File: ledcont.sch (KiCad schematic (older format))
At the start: 22 parts, among them J1 Screw_Terminal_01x02, J2 Screw_Terminal_01x02, U1 PAM2804, U2 TSM102A

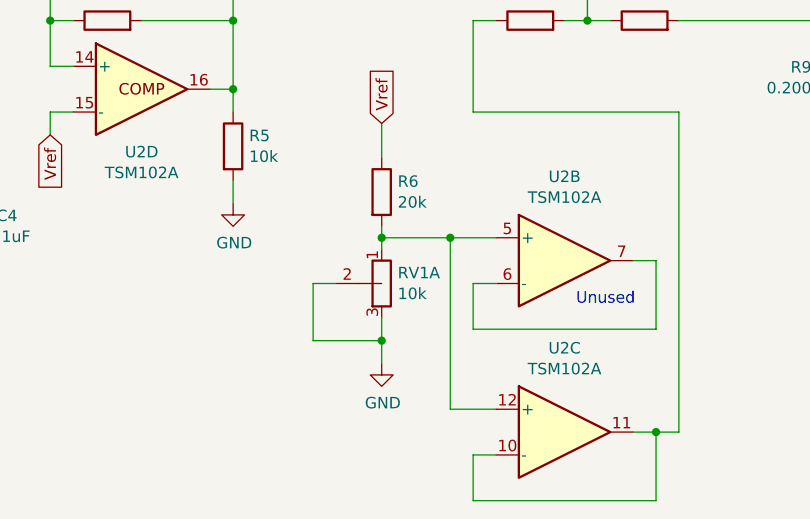
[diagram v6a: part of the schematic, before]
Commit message: Reverse potentionmeter usage so that the LEDs start out dimmed.
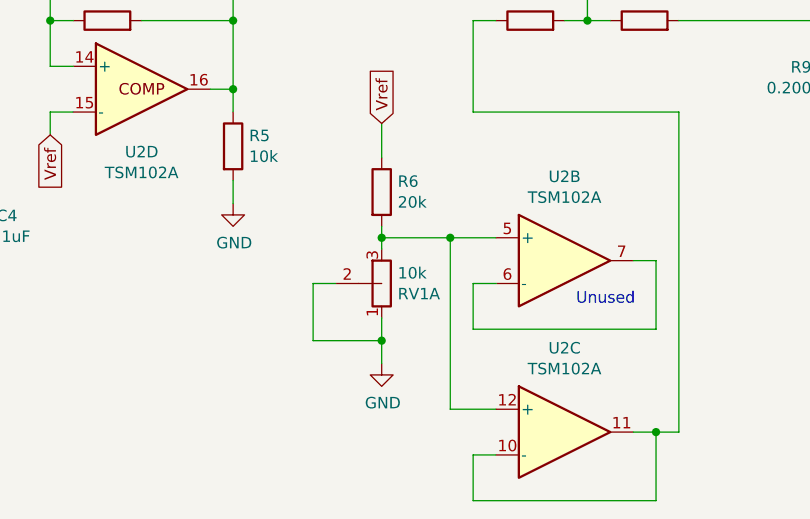
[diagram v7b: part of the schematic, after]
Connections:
- net GND: now also RV1.1; no longer RV1.3
- net at R6.2, U2.12 (+), U2.5 (+): now also RV1.3; no longer RV1.1
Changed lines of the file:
@@
 F 4 "P091S-FC20BR10K" H 0   0   50  0001 C CNN "Part"
 	1    6750 4200
-	-1   0    0    1
+	-1   0    0    -1
 $EndComp
 $Comp

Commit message: Remove this note.
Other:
- note removed: "XXX -\nLet's always drive the output low? Is this right?"
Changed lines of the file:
@@
 Wire Wire Line
 	2950 3500 2550 3500
-Text Notes 2150 3150 0    50   ~ 0
-XXX -\nLet's always drive the output low?  Is this right?
 Wire Notes Line
 	2300 1750 2300 2650
